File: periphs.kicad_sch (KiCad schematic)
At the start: 1 part, among them U501 STM32L552ZET6Q

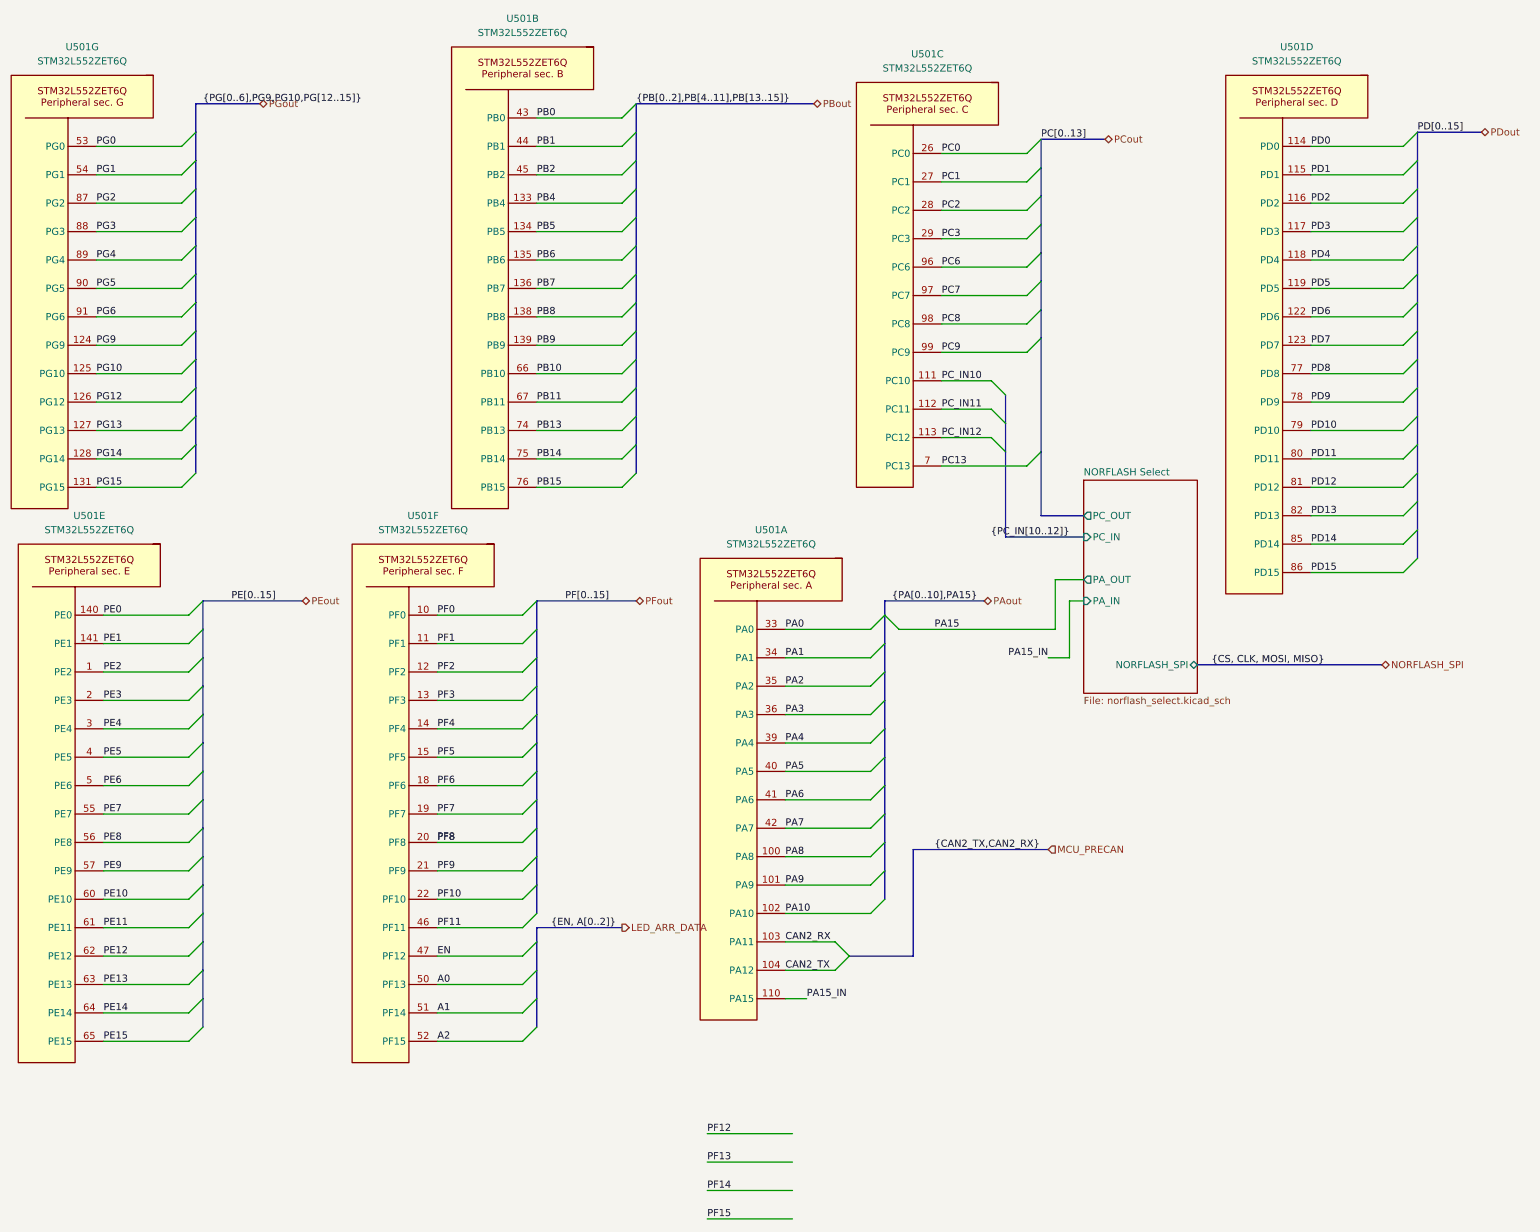
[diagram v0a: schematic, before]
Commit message: small schematic changes, need to reroute
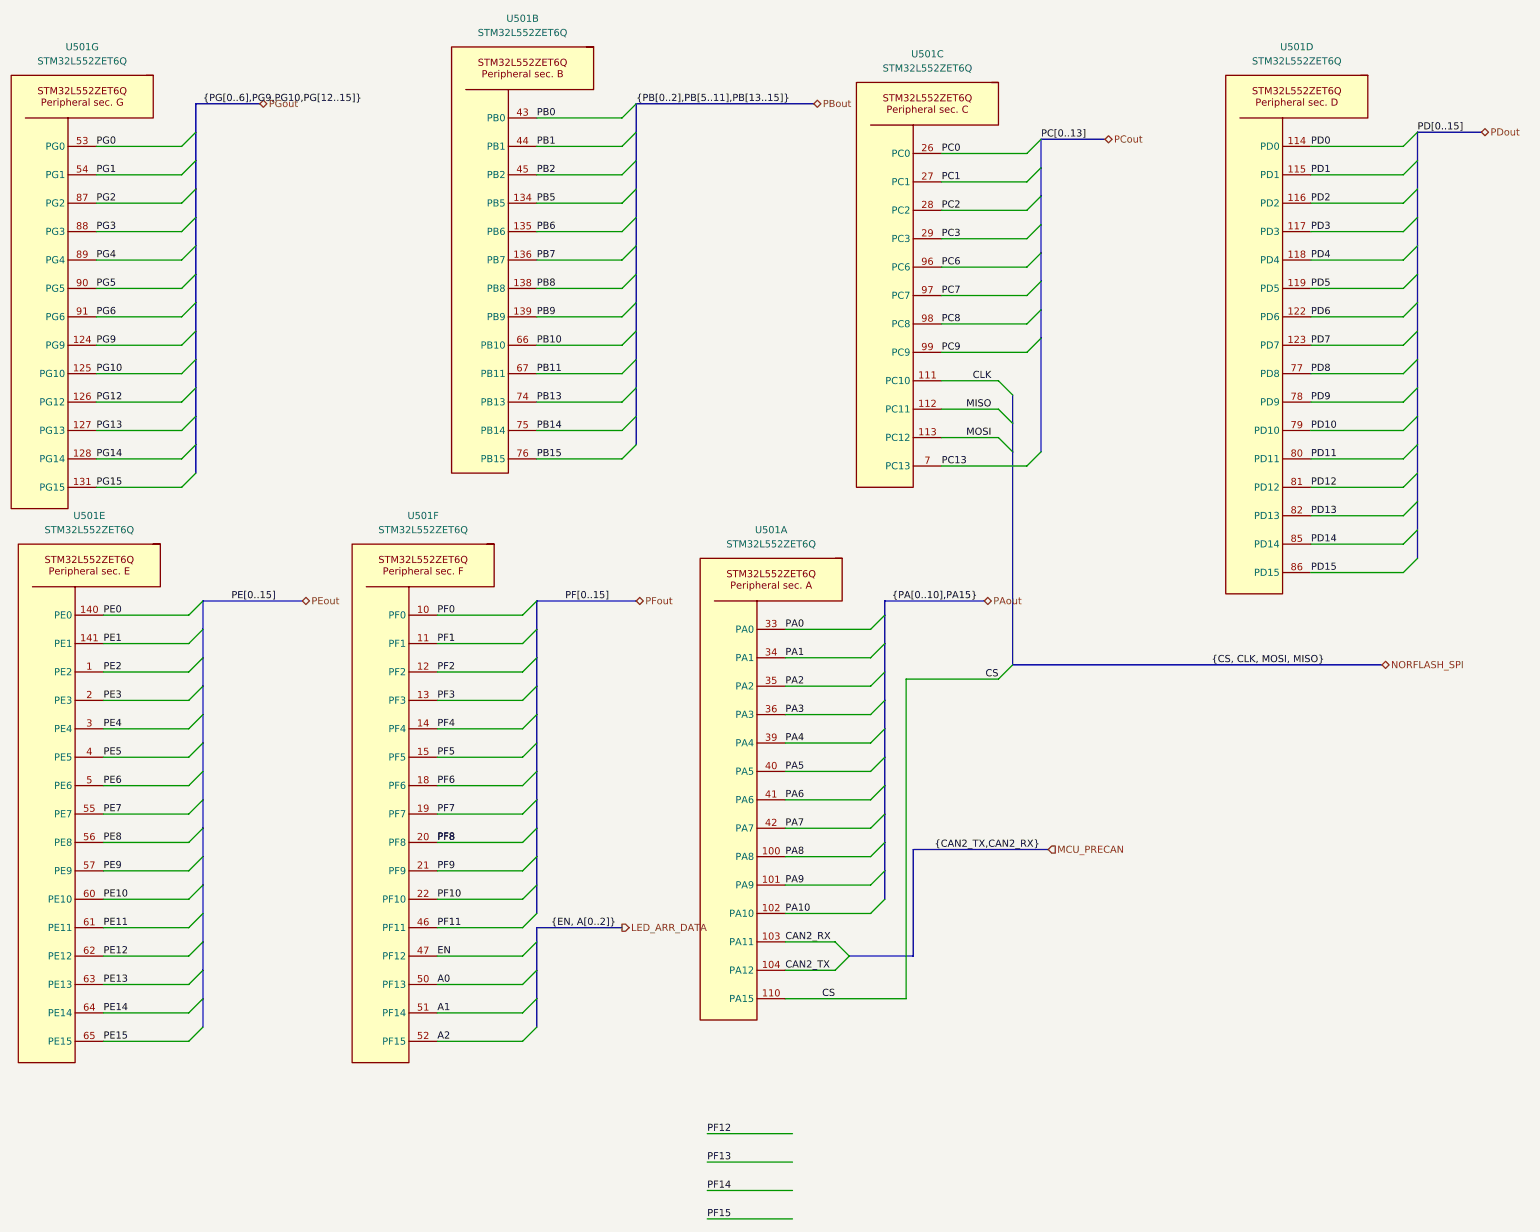
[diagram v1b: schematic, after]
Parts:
- removed unit 2 of U501
- added unit 2 of U501
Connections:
- net PB0: now also U501.43 (PB0)
- net PB1: now also U501.44 (PB1)
- net PB10: now also U501.66 (PB10)
- net PB11: now also U501.67 (PB11)
- net PB13: now also U501.74 (PB13)
- net PB14: now also U501.75 (PB14)
- net PB15: now also U501.76 (PB15)
- net PB2: now also U501.45 (PB2)
- net PB5: now also U501.134 (PB5)
- net PB6: now also U501.135 (PB6)
- net PB7: now also U501.136 (PB7)
- net PB8: now also U501.138 (PB8)
- net PB9: now also U501.139 (PB9)
- net PA15_IN renamed CS
- net PC_IN10 renamed CLK
- net PC_IN11 renamed MISO
- net PC_IN12 renamed MOSI
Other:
- removed sheet NORFLASH Select
